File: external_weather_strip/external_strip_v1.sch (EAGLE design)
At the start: 10 parts, among them U1 ML8511-UV-SENSOR, U2 SHT21, U9 BMP180

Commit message: layouting 0.4
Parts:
- added U$5: MCP3425, phMeter:MCP3425
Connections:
- net ENABLE: no longer JP2.4
- net OUT: no longer JP2.3
- net SCL: now also JP2.4
- net SDA: now also JP2.3
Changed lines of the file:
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@@
 <part name="GND8" library="SparkFun-Aesthetics" deviceset="GND" device=""/>
 <part name="+3V4" library="supply1" deviceset="+3V3" device=""/>
+<part name="U$5" library="phMeter" deviceset="MCP3425" device=""/>
 </parts>
 <sheets>
@@
 <attribute name="VALUE" x="175.26" y="165.1" size="1.778" layer="96"/>
 </instance>
+<instance part="U$5" gate="G$1" x="53.34" y="20.32"/>
 </instances>
 <busses>
@@
 <junction x="63.5" y="58.42"/>
 </segment>
-<segment>
-<wire x1="43.18" y1="111.76" x2="38.1" y2="111.76" width="0.1524" layer="91"/>
-<label x="38.1" y="111.76" size="1.27" layer="95" rot="MR0" xref="yes"/>
-<pinref part="JP2" gate="G$1" pin="4"/>
-</segment>
 </net>
 <net name="OUT" class="0">
@@
 <wire x1="60.96" y1="48.26" x2="63.5" y2="48.26" width="0.1524" layer="91"/>
 <label x="63.5" y="48.26" size="1.27" layer="95" xref="yes"/>
-</segment>
-<segment>
-<wire x1="43.18" y1="114.3" x2="38.1" y2="114.3" width="0.1524" layer="91"/>
-<label x="38.1" y="114.3" size="1.27" layer="95" rot="MR0" xref="yes"/>
-<pinref part="JP2" gate="G$1" pin="3"/>
 </segment>
 </net>
@@
 <label x="106.68" y="137.16" size="1.778" layer="95"/>
 </segment>
+<segment>
+<wire x1="43.18" y1="114.3" x2="38.1" y2="114.3" width="0.1524" layer="91"/>
+<label x="38.1" y="114.3" size="1.27" layer="95" rot="MR0" xref="yes"/>
+<pinref part="JP2" gate="G$1" pin="3"/>
+</segment>
 </net>
 <net name="SCL" class="0">
@@
 <label x="106.68" y="132.08" size="1.778" layer="95"/>
 </segment>
-</net>
+<segment>
+<wire x1="43.18" y1="111.76" x2="38.1" y2="111.76" width="0.1524" layer="91"/>
+<label x="38.1" y="111.76" size="1.27" layer="95" rot="MR0" xref="yes"/>
+<pinref part="JP2" gate="G$1" pin="4"/>
+</segment>
+</net>

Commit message: finished weather strip
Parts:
- removed JP2: (no value), SparkFun-Connectors:M04PTH
- added C4: 100n, rcl:C-EUC0603
- added JP1: (no value), Headerlibrary:PINHD-1X5
- R1: value 10K -> 10k; device SparkFun-Resistors:10KOHM1/10W1%(0603)0603 -> resistor:R-EU_R0603
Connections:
- removed net 3.3V: C2.1, JP2.1, R1.2, U1.VDD
- removed net ENABLE: R1.1, U1.EN
- removed net OUT: U1.OUT
- new net N$1: U$5.VIN+, U1.OUT
- new net UV_EN: JP1.5, R1.1, U1.EN
- net +3V3: now also C2.1, C4.1, JP1.1, U$5.VDD, U1.VDD
- net GND: now also C4.2, JP1.2, R1.2, U$5.VIN-, U$5.VSS; no longer JP2.2
- net SCL: now also JP1.4, U$5.SCL; no longer JP2.4
- net SDA: now also JP1.3, U$5.SDA; no longer JP2.3
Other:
- moved on the sheet: C1, C2, U1

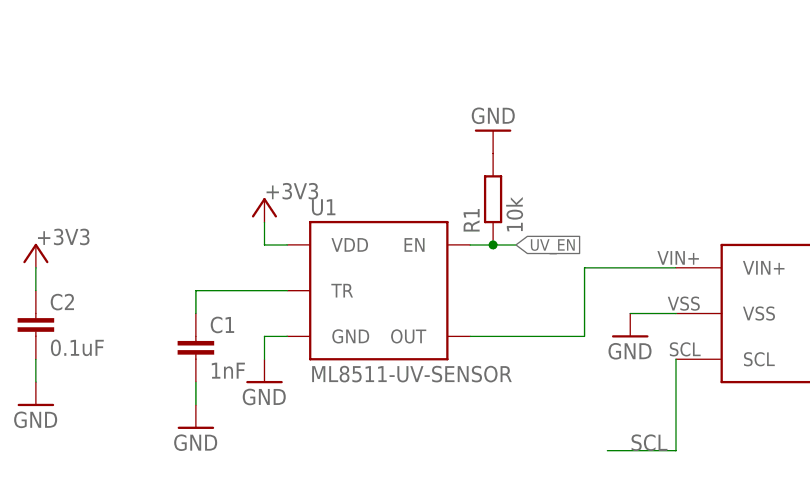
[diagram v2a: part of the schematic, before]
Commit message: corrected UV sensor footprint
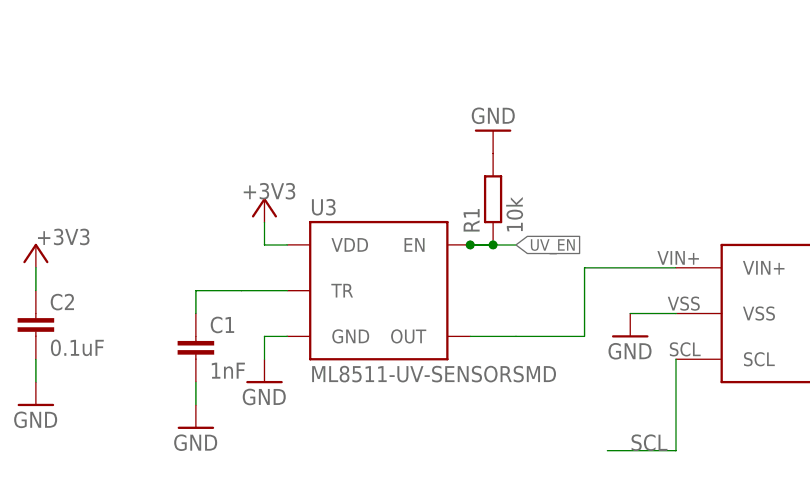
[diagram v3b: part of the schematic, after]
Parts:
- removed U1: ML8511-UV-SENSOR, ML8511:ML8511-UV-SENSORSMD
- added U3: ML8511-UV-SENSORSMD, SparkFun-Sensors:ML8511-UV-SENSORSMD
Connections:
- net +3V3: now also U3.VDD; no longer U1.VDD
- net GND: now also U3.GND; no longer U1.GND
- net N$1: now also U3.OUT; no longer U1.OUT
- net N$3: now also U3.TR; no longer U1.TR
- net UV_EN: now also U3.EN; no longer U1.EN
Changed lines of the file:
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@@
 <layer number="111" name="LPC17xx" color="7" fill="1" visible="yes" active="yes"/>
 <layer number="112" name="tSilk" color="7" fill="1" visible="yes" active="yes"/>
+<layer number="113" name="IDFDebug" color="7" fill="1" visible="yes" active="yes"/>
 <layer number="116" name="Patch_BOT" color="9" fill="4" visible="yes" active="yes"/>
 <layer number="118" name="Rect_Pads" color="4" fill="1" visible="yes" active="yes"/>
@@
 <layer number="127" name="_tValues" color="7" fill="1" visible="yes" active="yes"/>
 <layer number="128" name="_bValues" color="7" fill="1" visible="yes" active="yes"/>
+<layer number="129" name="Mask" color="7" fill="1" visible="yes" active="yes"/>
 <layer number="131" name="tAdjust" color="7" fill="1" visible="yes" active="yes"/>
 <layer number="132" name="bAdjust" color="7" fill="1" visible="yes" active="yes"/>
@@
 <layer number="223" name="223bmp" color="24" fill="1" visible="no" active="no"/>
 <layer number="224" name="224bmp" color="25" fill="1" visible="no" active="no"/>
+<layer number="225" name="225bmp" color="7" fill="1" visible="yes" active="yes"/>
+<layer number="226" name="226bmp" color="7" fill="1" visible="yes" active="yes"/>
+<layer number="227" name="227bmp" color="7" fill="1" visible="yes" active="yes"/>
+<layer number="228" name="228bmp" color="7" fill="1" visible="yes" active="yes"/>
+<layer number="229" name="229bmp" color="7" fill="1" visible="yes" active="yes"/>
+<layer number="230" name="230bmp" color="7" fill="1" visible="yes" active="yes"/>
+<layer number="231" name="231bmp" color="7" fill="1" visible="yes" active="yes"/>
 <layer number="248" name="Housing" color="7" fill="1" visible="yes" active="yes"/>
 <layer number="249" name="Edge" color="7" fill="1" visible="yes" active="yes"/>
@@
 <layer number="251" name="SMDround" color="7" fill="1" visible="no" active="no"/>
 <layer number="254" name="cooling" color="7" fill="1" visible="yes" active="yes"/>
+<layer number="255" name="routoute" color="7" fill="1" visible="yes" active="yes"/>
 </layers>
 <schematic xreflabel="%F%N/%S.%C%R" xrefpart="/%S.%C%R">
@@
 </classes>
 <parts>
-<part name="U1" library="ML8511" deviceset="ML8511-UV-SENSOR" device="SMD" value="ML8511-UV-SENSOR"/>
 <part name="GND1" library="SparkFun-Aesthetics" deviceset="GND" device=""/>
 <part name="GND2" library="SparkFun-Aesthetics" deviceset="GND" device=""/>
@@
 <part name="+3V3" library="supply1" deviceset="+3V3" device=""/>
 <part name="+3V5" library="supply1" deviceset="+3V3" device=""/>
+<part name="U3" library="SparkFun-Sensors" deviceset="ML8511-UV-SENSOR" device="SMD"/>
 </parts>
 <sheets>
@@
 </plain>
 <instances>
-<instance part="U1" gate="U1" x="25.4" y="50.8"/>
 <instance part="GND1" gate="1" x="40.64" y="106.68" rot="MR0"/>
 <instance part="GND2" gate="1" x="12.7" y="40.64"/>
@@
 </instance>
 <instance part="+3V2" gate="G$1" x="12.7" y="60.96" smashed="yes">
-<attribute name="VALUE" x="12.7" y="60.96" size="1.778" layer="96"/>
+<attribute name="VALUE" x="10.16" y="60.96" size="1.778" layer="96"/>
 </instance>
 <instance part="+3V3" gate="G$1" x="99.06" y="71.12" smashed="yes">
@@
 <attribute name="VALUE" x="40.64" y="124.46" size="1.778" layer="96"/>
 </instance>
+<instance part="U3" gate="U1" x="25.4" y="50.8"/>
 </instances>
 <busses>
@@
 <net name="GND" class="0">
 <segment>
-<pinref part="U1" gate="U1" pin="GND"/>
 <pinref part="GND2" gate="1" pin="GND"/>
 <wire x1="15.24" y1="45.72" x2="12.7" y2="45.72" width="0.1524" layer="91"/>
 <wire x1="12.7" y1="45.72" x2="12.7" y2="43.18" width="0.1524" layer="91"/>
+<pinref part="U3" gate="U1" pin="GND"/>
 </segment>
 <segment>
@@
 <net name="UV_EN" class="0">
 <segment>
-<pinref part="U1" gate="U1" pin="EN"/>
 <label x="40.64" y="55.88" size="1.27" layer="95" xref="yes"/>
 <wire x1="35.56" y1="55.88" x2="38.1" y2="55.88" width="0.1524" layer="91"/>
@@
 <wire x1="38.1" y1="55.88" x2="40.64" y2="55.88" width="0.1524" layer="91"/>
 <junction x="38.1" y="55.88"/>
+<wire x1="38.1" y1="55.88" x2="35.56" y2="55.88" width="0.1524" layer="91"/>
+<pinref part="U3" gate="U1" pin="EN"/>
+<junction x="35.56" y="55.88"/>
 </segment>
 <segment>
@@
 <net name="N$3" class="0">
 <segment>
-<pinref part="U1" gate="U1" pin="TR"/>
-<wire x1="15.24" y1="50.8" x2="5.08" y2="50.8" width="0.1524" layer="91"/>
+<wire x1="15.24" y1="50.8" x2="10.16" y2="50.8" width="0.1524" layer="91"/>
+<wire x1="10.16" y1="50.8" x2="5.08" y2="50.8" width="0.1524" layer="91"/>
 <wire x1="5.08" y1="50.8" x2="5.08" y2="48.26" width="0.1524" layer="91"/>
 <pinref part="C1" gate="G$1" pin="1"/>
+<pinref part="U3" gate="U1" pin="TR"/>
 </segment>
 </net>
@@
 </segment>
 <segment>
-<pinref part="U1" gate="U1" pin="VDD"/>
 <wire x1="15.24" y1="55.88" x2="12.7" y2="55.88" width="0.1524" layer="91"/>
 <wire x1="12.7" y1="55.88" x2="12.7" y2="58.42" width="0.1524" layer="91"/>
 <pinref part="+3V2" gate="G$1" pin="+3V3"/>
+<pinref part="U3" gate="U1" pin="VDD"/>
 </segment>
 <segment>
@@
 <pinref part="U$5" gate="G$1" pin="VIN+"/>
 <wire x1="58.42" y1="53.34" x2="48.26" y2="53.34" width="0.1524" layer="91"/>
-<pinref part="U1" gate="U1" pin="OUT"/>
 <wire x1="48.26" y1="53.34" x2="48.26" y2="45.72" width="0.1524" layer="91"/>
-<wire x1="48.26" y1="45.72" x2="35.56" y2="45.72" width="0.1524" layer="91"/>
-</segment>
-</net>
+<wire x1="48.26" y1="45.72" x2="40.64" y2="45.72" width="0.1524" layer="91"/>
+<wire x1="40.64" y1="45.72" x2="35.56" y2="45.72" width="0.1524" layer="91"/>
+<pinref part="U3" gate="U1" pin="OUT"/>
+</segment>
+</net>

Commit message: finished weather strip
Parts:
- added BLP, RST: PTR1B1,27, testpad:PTR1B1,27
- added C10: 12p, rcl:C-EUC0603
- added C13: 10u, rcl:C-EUC0603
- added C14: 670p, rcl:C-EUC0603
- added C15: 270p, rcl:C-EUC0603
- added C16: 10uF, SparkFun-Retired:10UF-TANT
- added C5: 1n, SparkFun-Capacitors:1NF/1000PF-50V-10%(0603)
- added C6, C7, C8: 100n, rcl:C-EUC0603
- added C9: 120n, rcl:C-EUC0603
- added IC1: AS3935, AS3935:AS3935
- added IC2: BNO055A, BNO055:BNO055A
- added L1: 100uH, AS3935:COILCRAFT
- added Q1: 32.768kHz, crystal:FC-12M
- added R2, R3: 10k, rcl:R-EU_R0603
- added R4: 10k, resistor:R-EU_R0603
- C1: value 1nF -> 100n; device SparkFun-Capacitors:1NF/1000PF-50V-10%(0603) -> rcl:C-EUC0603
- C11: value 100n -> 12p
- C12: value 10u -> 1u; device resistor:CPOL-EUA/3216-18R -> rcl:C-EUC0603
- C2: value 0.1uF -> 100n; device SparkFun-Capacitors:0.1UF-25V(+80/-20%)(0603) -> rcl:C-EUC0603
- C4: device rcl:C-EUC0603 -> SparkFun-Capacitors:0.1UF-25V(+80/-20%)(0603)
- JP1: device Headerlibrary:PINHD-1X5 -> pinhead:PINHD-1X7
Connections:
- new net ACCEL_IRQ: IC2.INT, JP1.7
- new net ACCEL_N_BOOTLD: BLP.TP, IC2.BOOT_LOAD_PIN, R3.1
- new net ACCEL_N_RST: IC2.RESET, R2.2, RST.TP
- new net LIGHTNING_IRQ: IC1.IRQ, JP1.6
- new net N$18: C7.2, IC2.CAP
- new net N$19: C10.1, IC2.XIN32, Q1.2
- new net N$2: C13.2, IC1.ACG
- new net N$5: C14.1, C15.1, IC1.INP, L1.1, R4.2
- new net N$73: C11.1, IC2.XOUT32, Q1.1
- net +3V3: now also C1.1, C12.2, C16.+, C6.1, C8.1, C9.1, IC1.ADD0, IC1.ADD1, IC1.SI, IC1.VDD, IC1.VREG, IC2.COM3, IC2.VDD, IC2.VDDIO, R2.1, R3.2; no longer C11.1, C12.+
- net GND: now also C10.2, C12.1, C13.1, C14.2, C15.2, C16.-, C5.2, C6.2, C7.1, C8.2, C9.2, IC1.EN_VREG, IC1.EXPAD, IC1.GND, IC1.INN, IC2.COM2, IC2.GND, IC2.GNDIO, IC2.PIN10, IC2.PIN15, IC2.PIN16, IC2.PS0, IC2.PS1, L1.2, R4.1; no longer C12.-
- net N$3: now also C5.1; no longer C1.1
- net SCL: now also IC1.I2CL/SCL, IC2.COM1
- net SDA: now also IC1.I2CD/MOSI, IC2.COM0
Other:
- note added: "COM3 high: I2C address 0x29 selected"
- note added: "Gyroscope/Accelerometer/Magnetometer"
- moved on the sheet: C1, C11, C2, C3, C4, R1, U2, U3, U9

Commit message: finished revised weather strip
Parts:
- renumbered IC1 to U6, IC2 to U5, U$5 to U4, U9 to U1
